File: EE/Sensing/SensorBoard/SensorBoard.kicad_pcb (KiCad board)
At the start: 2 copper layers, 113 parts, among them J1 Conn_02x13_Odd_Even, J101 Peg, J102 Peg, J11 Peg, J12 Peg, J21 Peg, J22 Peg, J31 Peg, J32 Peg, J41 Peg, J42 Peg, J51 Peg, J52 Peg, J61 Peg, J62 Peg, J71 Peg, J72 Peg, J81 Peg, J82 Peg, J91 Peg, J92 Peg, Q1 BSS84DW, Q10 BSS84DW, Q2 BSS84DW, Q3 BSS84DW, Q4 BSS84DW, Q5 BSS84DW, Q6 BSS84DW, Q7 BSS84DW, Q8 BSS84DW, Q9 BSS84DW, U1 TCR2EE27, U101 AH1381, U102 AH1381, U11 AH1381, U12 AH1381, U2 TCR2EE32, U21 AH1381, U22 AH1381, U31 AH1381, U32 AH1381, U41 AH1381, U42 AH1381, U51 AH1381, U52 AH1381, U61 AH1381, U62 AH1381, U71 AH1381, U72 AH1381, U81 AH1381, U82 AH1381, U91 AH1381, U92 AH1381

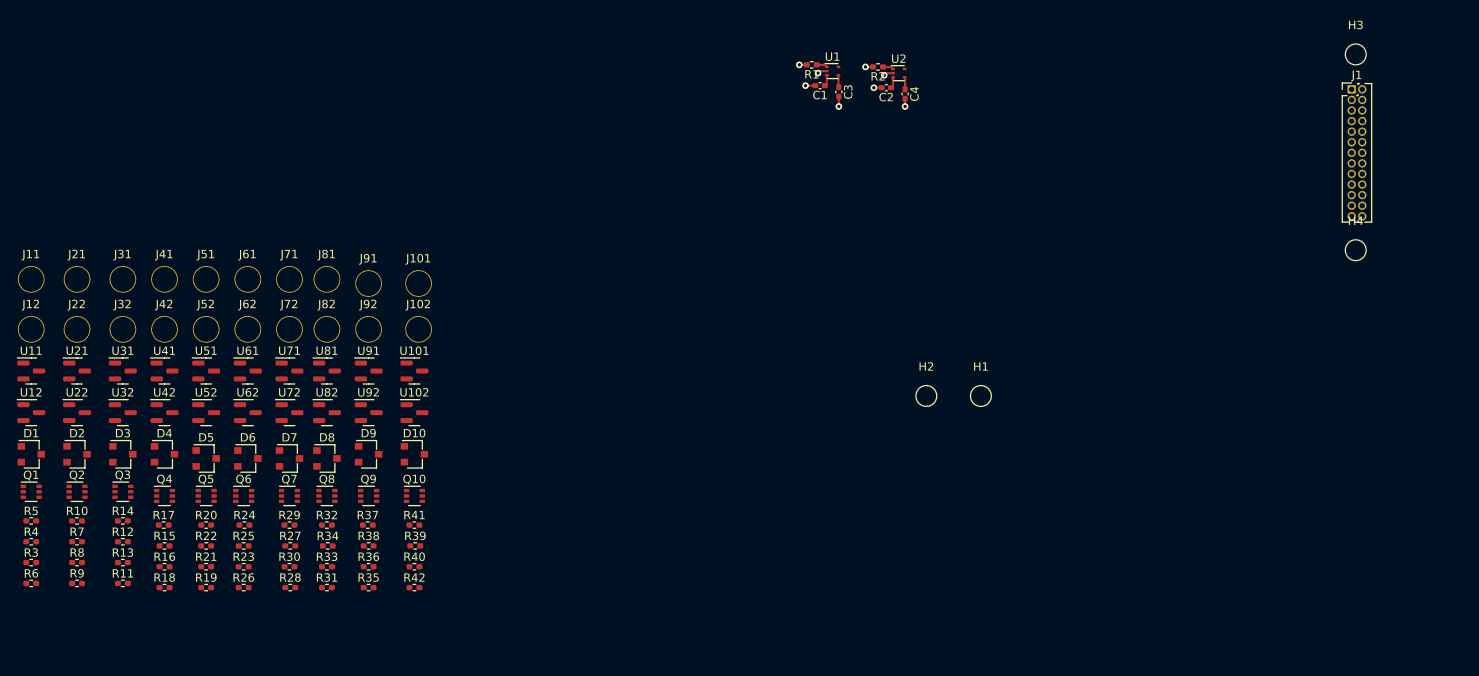
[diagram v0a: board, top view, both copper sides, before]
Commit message: First pass layout of LEDs/ Sensors
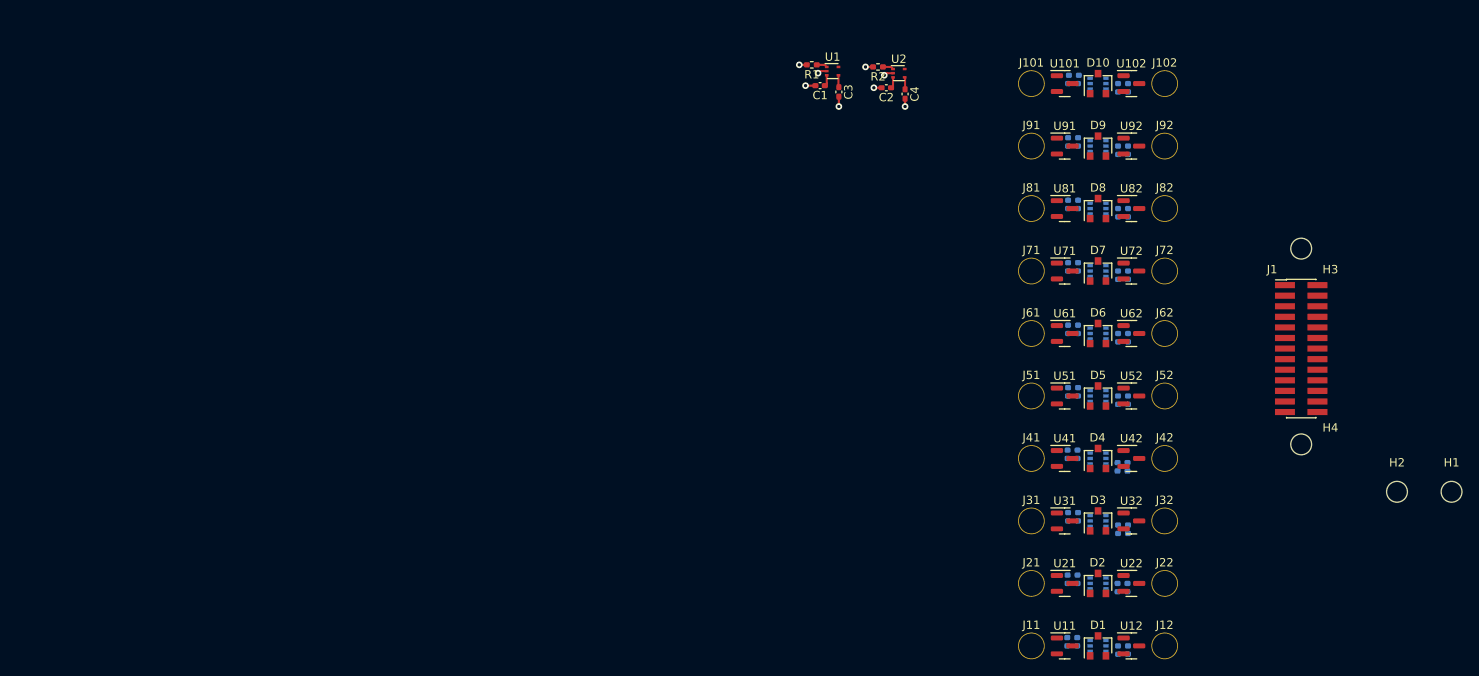
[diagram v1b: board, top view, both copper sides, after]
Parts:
- J1: footprint Connector_PinHeader_1.27mm:PinHeader_2x13_P1.27mm_Vertical -> Connector_PinHeader_1.27mm:PinHeader_2x13_P1.27mm_Vertical_SMD
- Q1, Q10, Q2, Q3, Q4, Q5, Q6, Q7, Q8, Q9, R10, R11, R12, R13, R14, R15, R16, R17, R18, R19, R20, R21, R22, R23, R24, R25, R26, R27, R28, R29, R3, R30, R31, R32, R33, R34, R35, R36, R37, R38, R39, R4, R40, R41, R42, R5, R6, R7, R8, R9: moved to B.Cu
- moved J12 141.1 mm to (237.1, 89.5)
- moved U12 135.0 mm to (233.1, 90.0)
- moved J22 133.7 mm to (237.1, 81.0)
- moved R4 131.8 mm to (232.1, 91.0), turned to 180 degrees
- moved R6 131.3 mm to (232.1, 90.0), turned to 180 degrees
- moved D1 130.1 mm to (229.1, 90.0), turned to 90 degrees
- moved Q1 129.4 mm to (229.1, 90.0)
- moved U11 128.4 mm to (225.1, 90.0)
- moved U22 128.2 mm to (233.1, 82.5)
- moved J11 127.5 mm to (221.1, 89.0)
- moved J32 127.1 mm to (237.1, 74.5)
- moved R5 125.7 mm to (226.0, 89.0), turned to 180 degrees
- moved R10 125.7 mm to (232.0, 82.5), turned to 180 degrees
- moved R8 125.5 mm to (232.0, 83.5), turned to 180 degrees
- moved R3 125.4 mm to (226.0, 90.0)
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
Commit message: More Layout
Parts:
- turned R31 to 0 degrees
- turned R32 to 180 degrees
- turned R36 to 180 degrees
- turned R5 to 0 degrees
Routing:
- net /2v7: track 2.91 -> 127.5 mm, vias 0 -> 20
- net GND: track 8.34 -> 45.9 mm, vias 8 -> 28
- net /B1_0_4: track 0.00 -> 4.42 mm, vias 0 -> 1
- net /B1_0_3: track 0.00 -> 4.42 mm, vias 0 -> 1
- net /B1_0_2: track 0.00 -> 4.42 mm, vias 0 -> 1
- net /B1_0_1: track 0.00 -> 4.42 mm, vias 0 -> 1
- net /B1_0_0: track 0.00 -> 4.42 mm, vias 0 -> 1
- net /B0_0_4: track 0.00 -> 4.42 mm, vias 0 -> 1
- net /B0_0_3: track 0.00 -> 4.42 mm, vias 0 -> 1
- net /B0_0_1: track 0.00 -> 4.42 mm, vias 0 -> 1
- net /B0_0_0: track 0.00 -> 4.42 mm, vias 0 -> 1
- net /B0_0_2: track 0.00 -> 4.38 mm, vias 0 -> 1
- net Net-(Q3-Pad6): track 0.00 -> 1.80 mm
- net Net-(Q4-Pad6): track 0.00 -> 1.74 mm
- net Net-(Q1-Pad3): track 0.00 -> 1.69 mm
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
